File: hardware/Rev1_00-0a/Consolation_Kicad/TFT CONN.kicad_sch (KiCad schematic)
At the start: 31 parts, among them J3 62684-402100ALF, U11 AP22913W6-7, U26 TPS61169DCKR

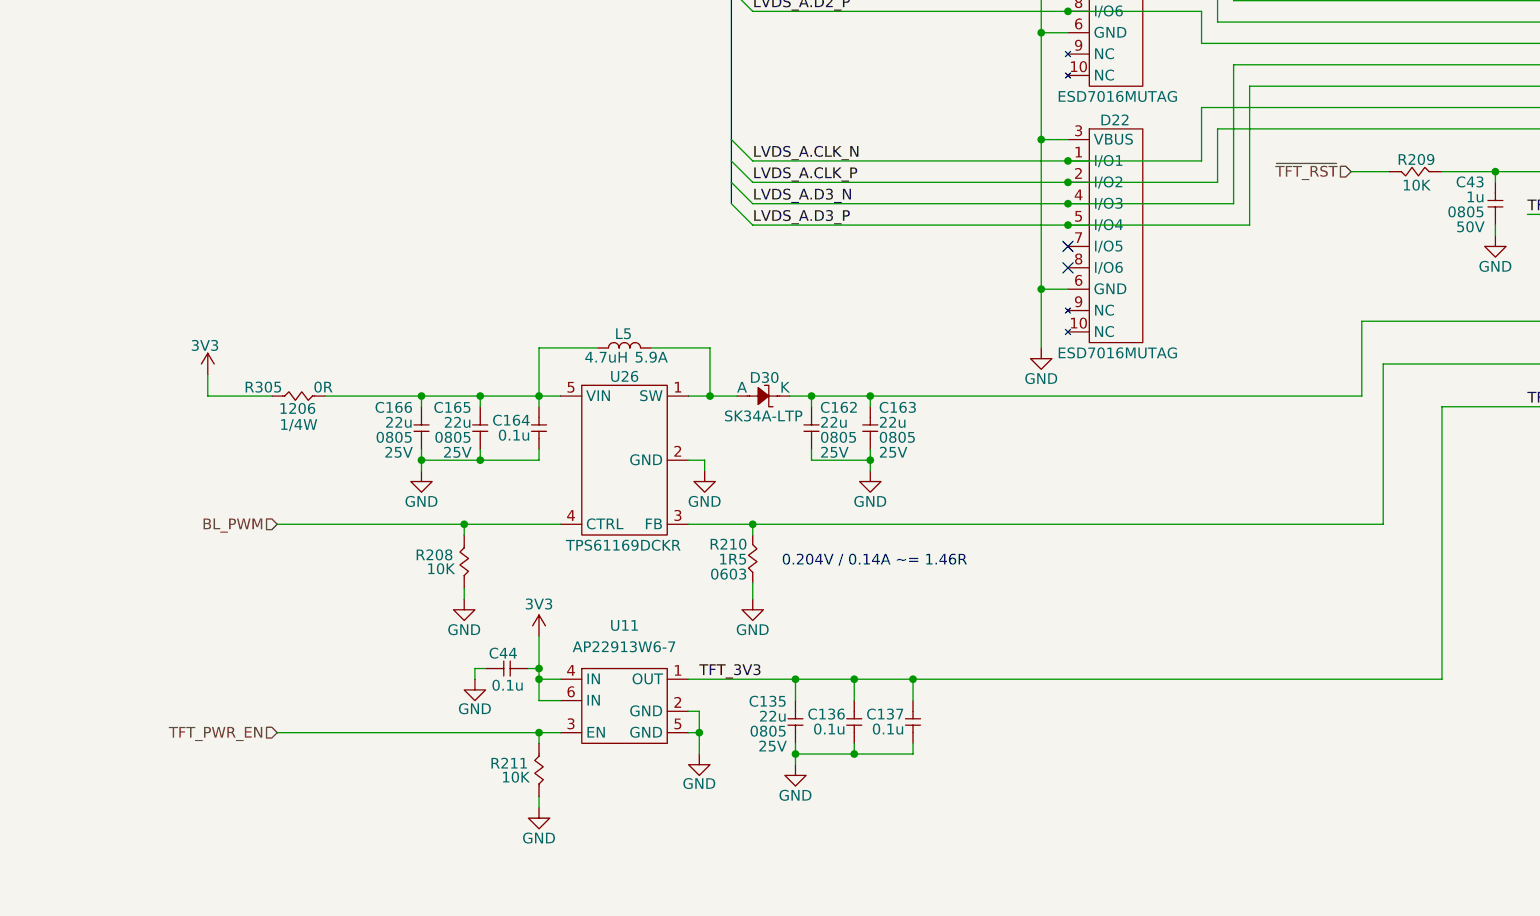
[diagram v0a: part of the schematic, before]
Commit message: Component preliminary placement
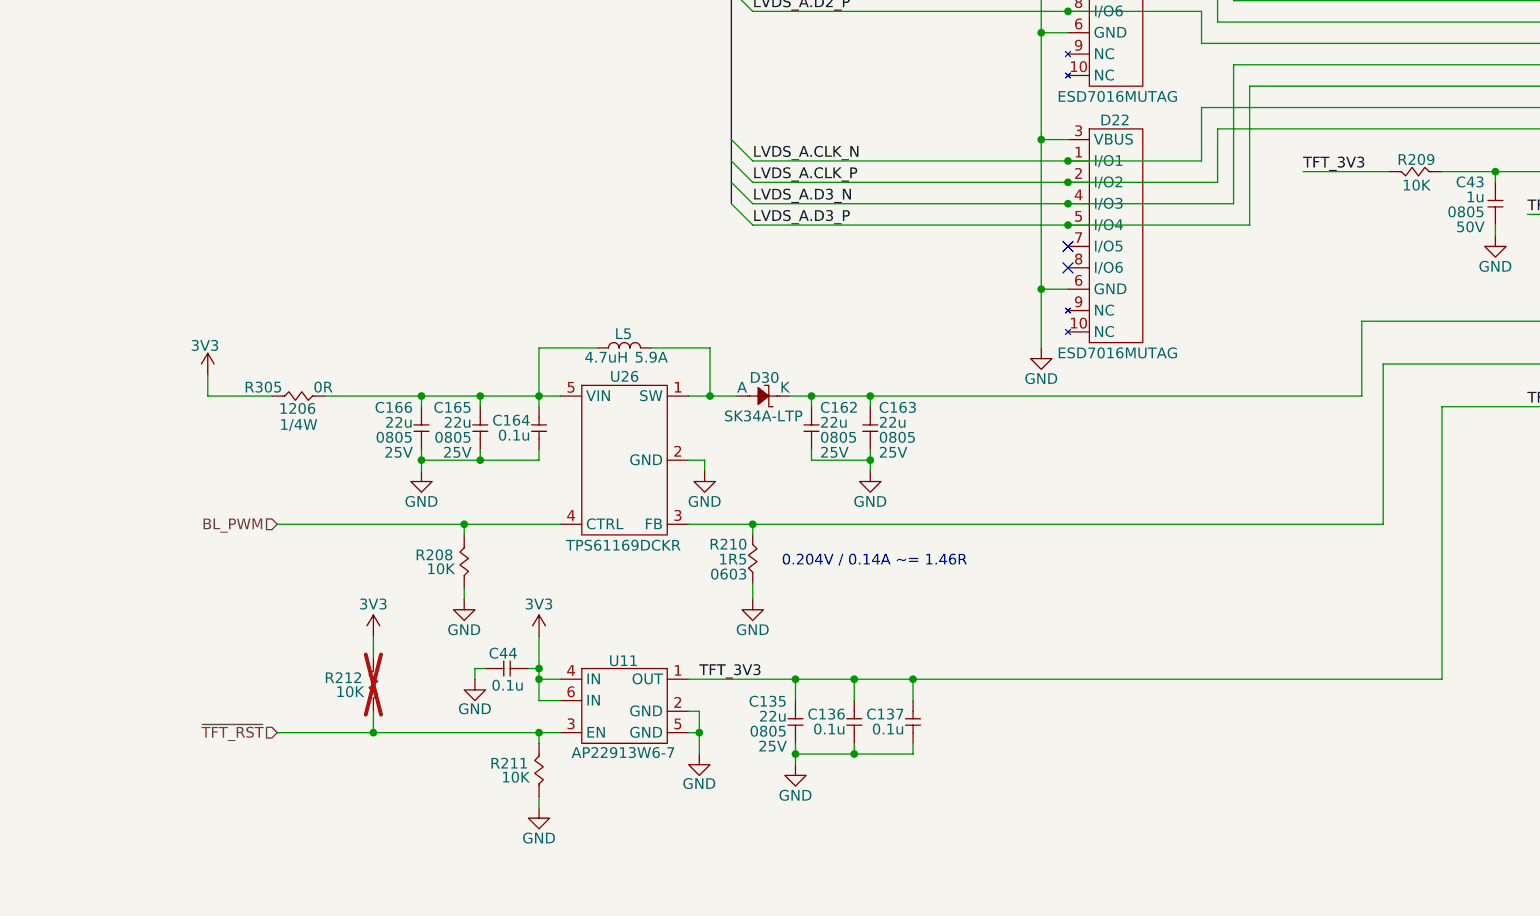
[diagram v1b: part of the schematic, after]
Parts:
- added R212: 10K, footprint:RES_0402, symbol KicadCompDb:Resistors/RES_SMT_00013
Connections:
- net TFT_PWR_EN is gone; now on net ~{TFT_RST}: R211.2, U11.3 (EN)
- net 3V3: now also R212.2
- net TFT_3V3: now also R209.2
- net ~{TFT_RST}: now also R212.1; no longer R209.2

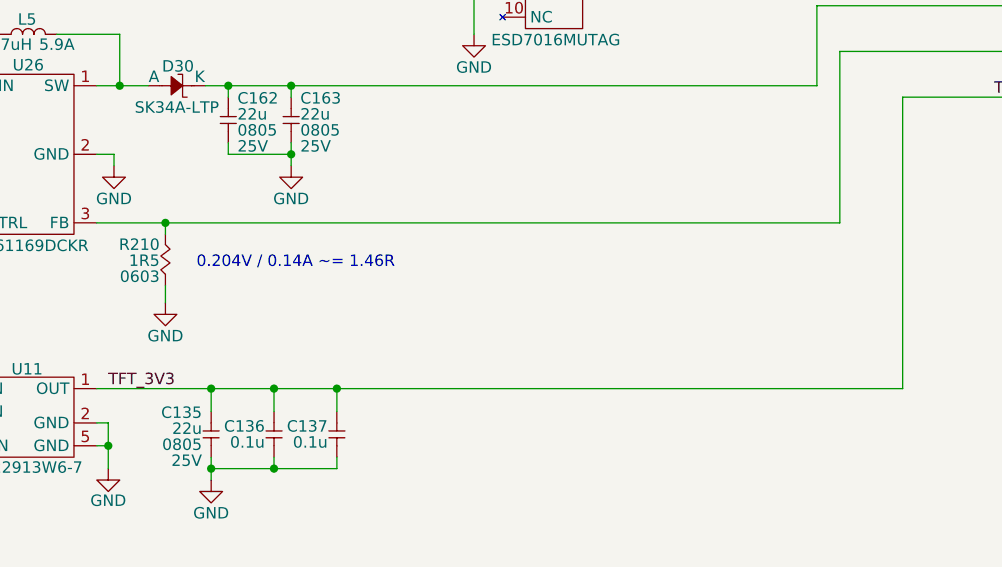
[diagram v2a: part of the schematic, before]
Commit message: Continue preliminary placement To do : Power supplies + Type C charger
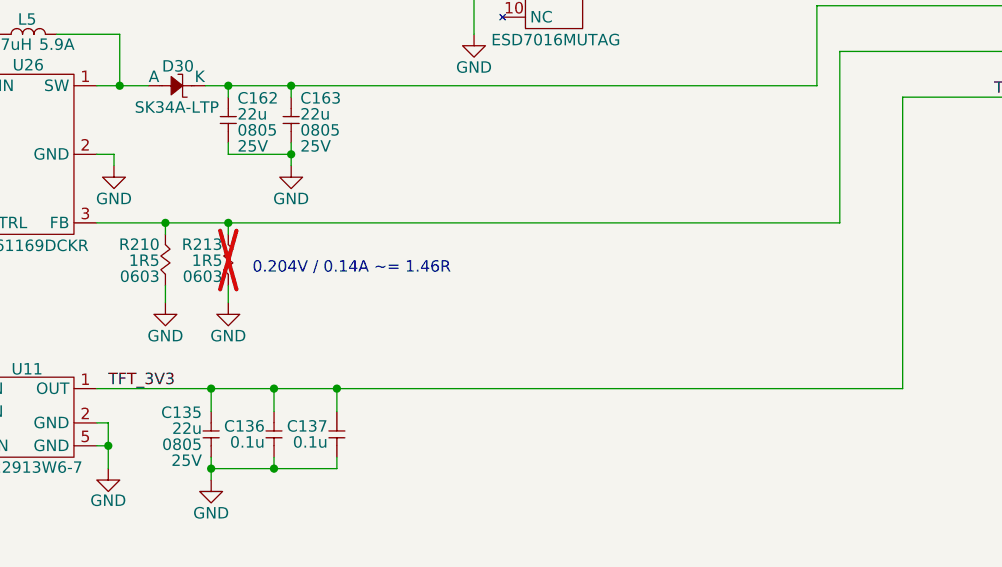
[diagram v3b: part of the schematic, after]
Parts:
- added R213: 1R5, footprint:RES_0603, symbol KicadCompDb:Resistors/RES_SMT_00007
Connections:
- net GND: now also R213.1
- net at J3.10 (LED-), J3.9 (LED-), R210.2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: now also R213.2

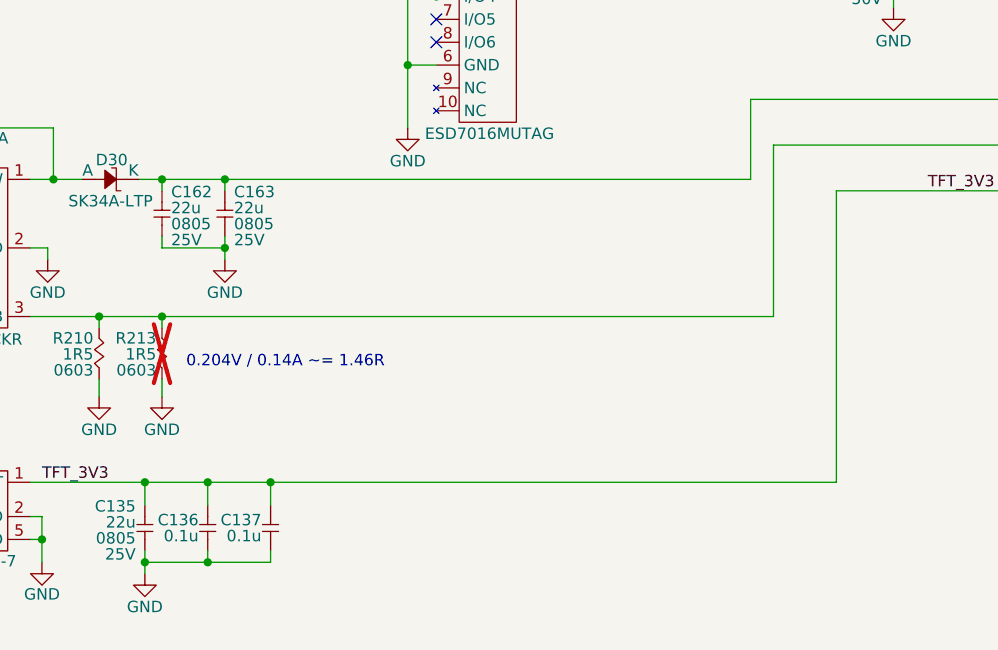
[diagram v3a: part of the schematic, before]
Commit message: Preliminary placement done Add test points to PCB
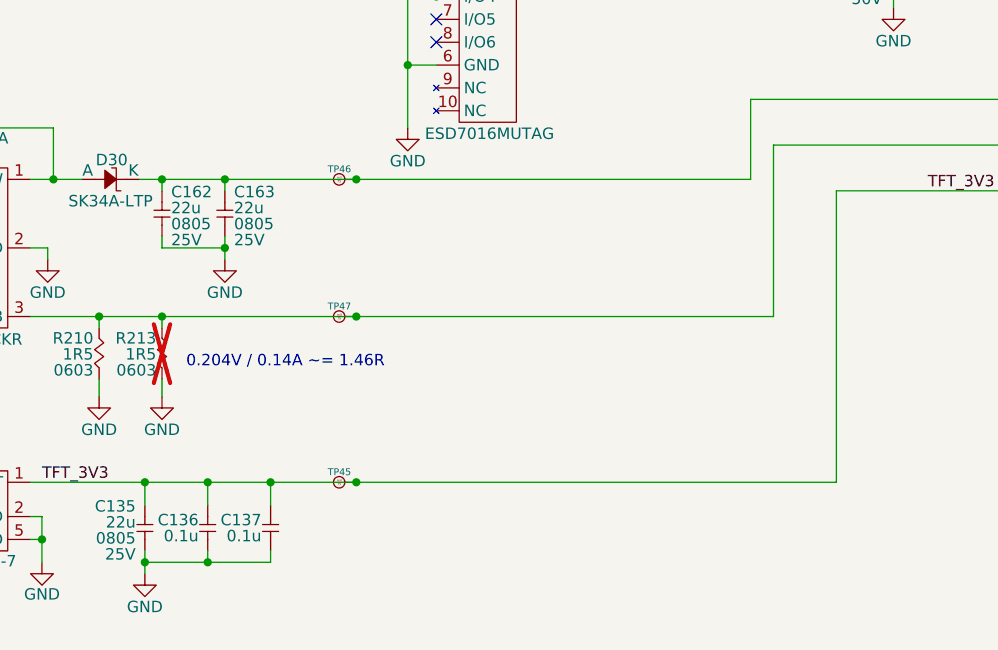
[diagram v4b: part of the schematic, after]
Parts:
- added TP45, TP46, TP47: 75 mils, footprint:SMT_TP_75_MILS, symbol KicadCompDb:Test Point/TP_00004
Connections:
- net TFT_3V3: now also TP45.1
- net at C162.2, C163.2, D30.1 (K)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: now also TP46.1
- net at J3.10 (LED-), J3.9 (LED-), R210.2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: now also TP47.1

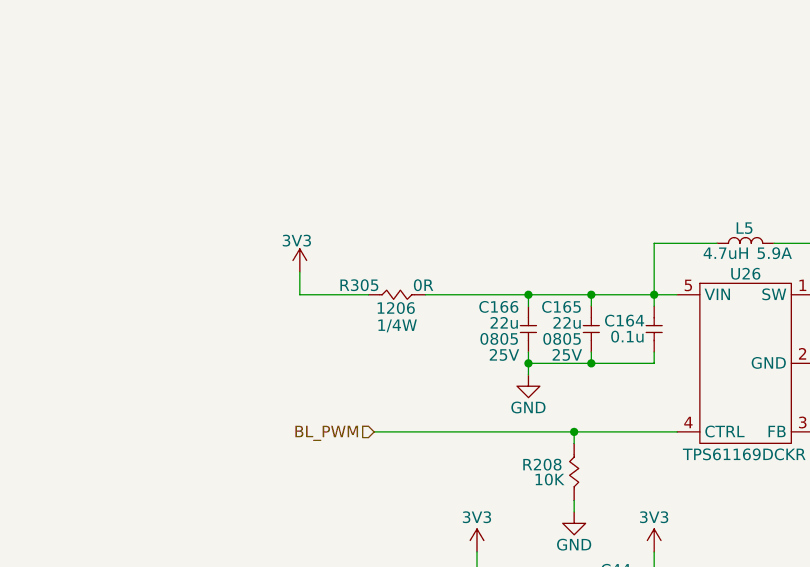
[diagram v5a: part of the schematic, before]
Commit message: Routing Adjust PinMux to ease routing
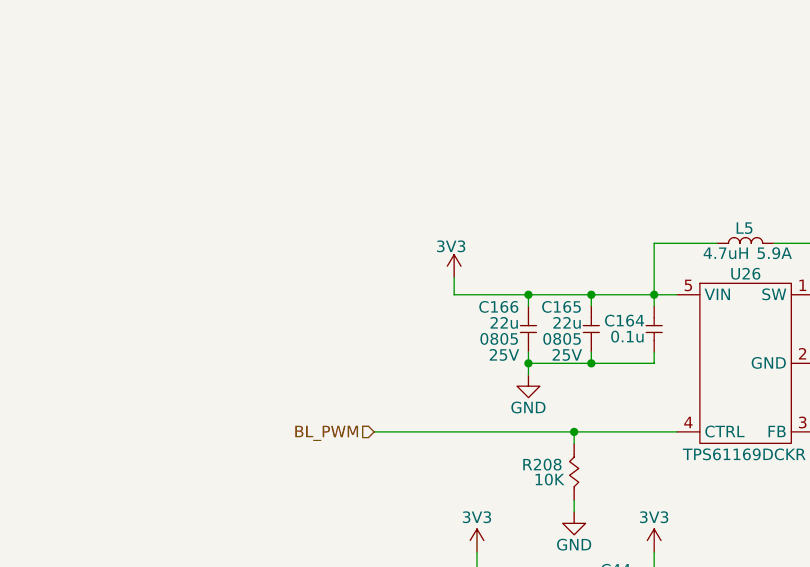
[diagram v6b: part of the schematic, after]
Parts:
- removed R305: 0R, footprint:RES_1206, symbol KicadCompDb:Resistors/RES_SMT_00022
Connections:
- net 3V3: now also C164.2, C165.2, C166.2, L5.1, U26.5 (VIN)
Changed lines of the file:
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@@
 	(title_block
 		(title "Consolation [Console Emulation]")
-		(date "2026-10-12")
+		(date "2026-10-25")
 		(rev "1.00-0A")
 		(comment 1 "Jean-Francois Bilodeau")
@@
 	(wire
 		(pts
-			(xy 81.915 91.44) (xy 81.915 93.98)
+			(xy 99.06 92.075) (xy 99.06 93.98)
 		)
 		(stroke
@@
 	(wire
 		(pts
-			(xy 81.915 93.98) (xy 89.535 93.98)
+			(xy 99.06 93.98) (xy 107.315 93.98)
 		)
 		(stroke
@@
 	(wire
 		(pts
-			(xy 95.885 93.98) (xy 107.315 93.98)
-		)
-		(stroke
-			(width 0)
-			(type default)
-		)
-	)
-	(wire
-		(pts
 			(xy 234.95 73.66) (xy 234.95 74.93)
 		)
@@
 	(symbol
 		(lib_id "KiCad_Pwr_Symbols:+3V3")
-		(at 81.915 91.44 0)
+		(at 99.06 92.075 0)
 		(unit 1)
 		(body_style 1)
@@
 		(dnp no)
 		(property "Reference" "#PWR0153"
-			(at 81.915 95.25 0)
+			(at 99.06 95.885 0)
 			(hide yes)
 			(show_name no)
@@
 		)
 		(property "Value" "3V3"
-			(at 79.883 88.011 0)
+			(at 97.028 88.646 0)
 			(show_name no)
 			(do_not_autoplace no)
@@
 		)
 		(property "Footprint" ""
-			(at 81.915 91.44 0)
+			(at 99.06 92.075 0)
 			(hide yes)
 			(show_name no)
@@
 		)
 		(property "Datasheet" ""
-			(at 81.915 91.44 0)
+			(at 99.06 92.075 0)
 			(hide yes)
 			(show_name no)
@@
 		)
 		(property "Description" "Power symbol creates a global label with name \"+3V3\""
-			(at 81.915 91.44 0)
+			(at 99.06 92.075 0)
 			(hide yes)
 			(show_name no)
@@
 					(unit 1)
 				)
-			)
-		)
-	)
-	(symbol
-		(lib_id "KicadCompDb:Resistors/RES_SMT_00022")
-		(at 90.805 93.98 0)
-		(unit 1)
-		(body_style 1)
-		(exclude_from_sim no)
-		(in_bom yes)
-		(on_board yes)
-		(in_pos_files yes)
-		(dnp no)
-		(property "Reference" "R305"
-			(at 88.519 92.964 0)
-			(show_name no)
-			(do_not_autoplace no)
-			(effects
-				(font
-					(size 1.27 1.27)
-				)
-			)
-		)
-		(property "Value" "0R"
-			(at 95.631 92.964 0)
-			(show_name no)
-			(do_not_autoplace no)
-			(effects
-				(font
-					(size 1.27 1.27)
-				)
-			)
-		)
-		(property "Footprint" "footprint:RES_1206"
-			(at 91.313 116.078 0)
-			(hide yes)
-			(show_name no)
-			(do_not_autoplace no)
-			(effects
-				(font
-					(size 1.27 1.27)
-				)
-			)
-		)
-		(property "Datasheet" "https://www.yageogroup.com/content/datasheet/asset/file/PYU-RC_GROUP_51_ROHS_L"
-			(at 90.805 93.98 0)
-			(hide yes)
-			(show_name no)
-			(do_not_autoplace no)
-			(effects
-				(font
-					(size 1.27 1.27)
-				)
-			)
-		)
-		(property "Description" "RES 0 OHM JUMPER 1/4W 1206"
-			(at 92.583 103.886 0)
-			(hide yes)
-			(show_name no)
-			(do_not_autoplace no)
-			(effects
-				(font
-					(size 1.27 1.27)
-				)
-			)
-		)
-		(property "Tolerance" "1%"
-			(at 92.71 88.9 0)
-			(hide yes)
-			(show_name no)
-			(do_not_autoplace no)
-			(effects
-				(font
-					(size 1.27 1.27)
-				)
-			)
-		)
-		(property "Power" "1/4W"
-			(at 92.71 97.409 0)
-			(show_name no)
-			(do_not_autoplace no)
-			(effects
-				(font
-					(size 1.27 1.27)
-				)
-			)
-		)
-		(property "Package" "1206"
-			(at 92.583 95.504 0)
-			(show_name no)
-			(do_not_autoplace no)
-			(effects
-				(font
-					(size 1.27 1.27)
-				)
-			)
-		)
-		(property "Manufacturer" "YAGEO"
-			(at 91.059 112.268 0)
-			(hide yes)
-			(show_name no)
-			(do_not_autoplace no)
-			(effects
-				(font
-					(size 1.27 1.27)
-				)
-			)
-		)
-		(property "Manufacturer Part Number" "RC1206JR-070RL"
-			(at 91.059 101.854 0)
-			(hide yes)
-			(show_name no)
-			(do_not_autoplace no)
-			(effects
-				(font
-					(size 1.27 1.27)
-				)
-			)
-		)
-		(property "Distributor" "DigiKey"
-			(at 90.805 99.822 0)
-			(hide yes)
-			(show_name no)
-			(do_not_autoplace no)
-			(effects
-				(font
-					(size 1.27 1.27)
-				)
-			)
-		)
-		(property "Distributor Part Number" "311-0.0ERCT-ND"
-			(at 91.567 106.172 0)
-			(hide yes)
-			(show_name no)
-			(do_not_autoplace no)
-			(effects
-				(font
-					(size 1.27 1.27)
-				)
-			)
-		)
-		(property "Temperature Coefficient" "±100ppm/°C"
-			(at 90.805 93.98 0)
-			(hide yes)
-			(show_name no)
-			(do_not_autoplace no)
-			(effects
-				(font
-					(size 1.27 1.27)
-				)
-			)
-		)
-		(property "Operating Temperature" "-55°C ~ 155°C"
-			(at 91.567 118.364 0)
-			(hide yes)
-			(show_name no)
-			(do_not_autoplace no)
-			(effects
-				(font
-					(size 1.27 1.27)
-				)
-			)
-		)
-		(property "Type" "RES SMT"
-			(at 90.805 93.98 0)
-			(hide yes)
-			(show_name yes)
-			(do_not_autoplace no)
-			(effects
-				(font
-					(size 1.27 1.27)
-				)
-			)
-		)
-		(property "Dimensions" "3.10mm x 1.60mm"
-			(at 90.805 93.98 0)
-			(hide yes)
-			(show_name yes)
-			(do_not_autoplace no)
-			(effects
-				(font
-					(size 1.27 1.27)
-				)
-			)
-		)
-		(pin "2"
-		)
-		(pin "1"
-		)
-		(instances
-			(project "Consolation_Kicad"
-				(path "/b18b5a64-cfe0-4447-acaf-556f3c6e6513/d6115ee7-6692-41e2-8017-fa08749ad748"
-					(reference "R305")
-					(unit 1)
-				)
